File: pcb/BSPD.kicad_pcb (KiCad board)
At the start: 4 copper layers, 45 x 63.7 mm, 61 parts, among them J1 Test header, J2 T4142012121-000, Q1 AO3400A, U1 LM339, U2 LM339, U3 74HC32, U4 LM339, U5 L7805, U6 L7805, U8 74HC1G04GV,125

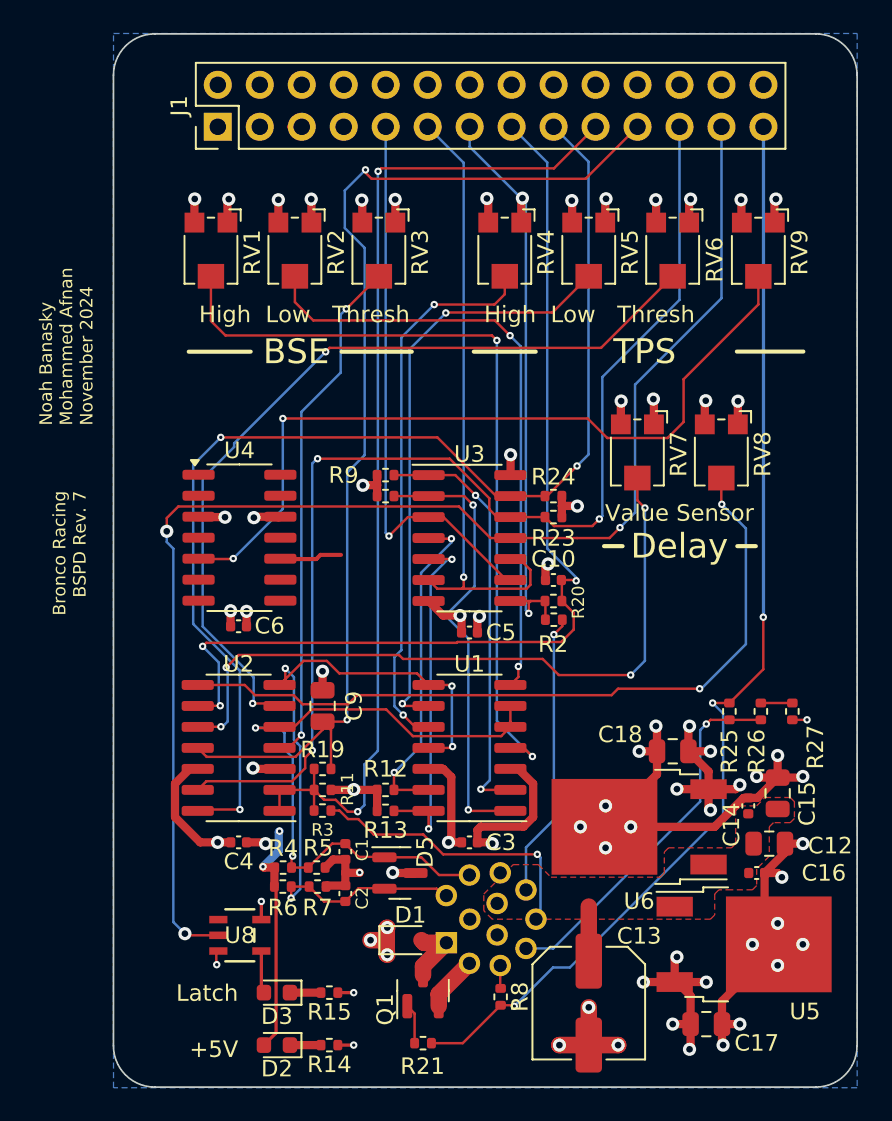
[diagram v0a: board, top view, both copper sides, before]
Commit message: change pcb layout
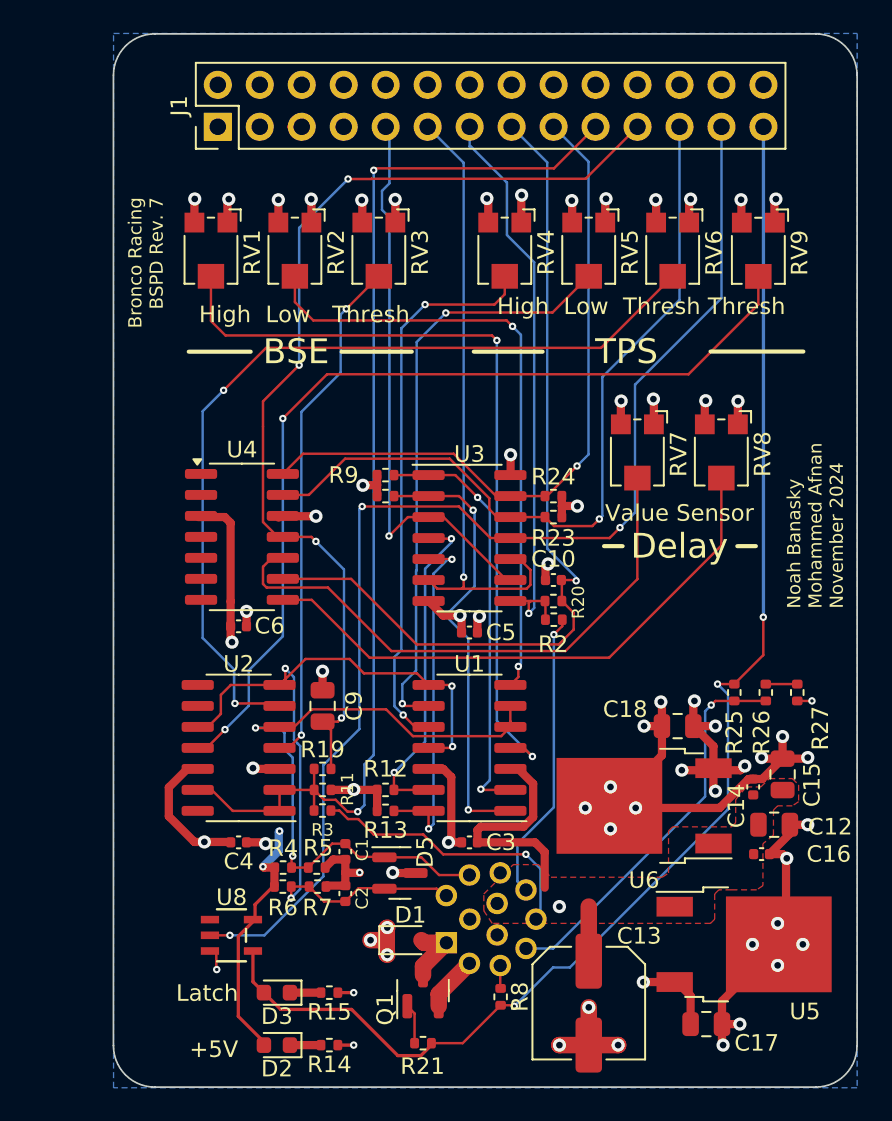
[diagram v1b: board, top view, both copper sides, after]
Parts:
- moved C18 1.55 mm to (146.6, 124.4)
- moved U6 1.31 mm to (144.6, 129.2)
- moved C12 1.18 mm to (152.5, 130.4)
- moved C14 1.18 mm to (151.2, 128.1)
- moved C15 1.18 mm to (153.0, 127.3)
- moved C16 1.18 mm to (151.7, 132.1)
- moved R25 1.18 mm to (150.1, 122.4)
- moved R26 1.18 mm to (152.0, 122.4)
- moved R27 1.18 mm to (153.9, 122.4)
- moved U8 0.51 mm to (119.6, 137.0)
- moved U4 0.16 mm to (120.3, 112.9)
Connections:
- U4 pad 10: SENSOR_DELAY -> VALUE_DELAY
- U4 pad 11: /Sensor Pre-Delay -> /Value Pre-Delay
- U4 pad 13: /Sensor Post-Delay -> /Value Post-Delay
- U4 pad 14: /Value Post-Delay -> /Sensor Post-Delay
- U4 pad 8: VALUE_DELAY -> SENSOR_DELAY
- U4 pad 9: /Value Pre-Delay -> /Sensor Pre-Delay
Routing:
- net Vin: track 24.9 -> 72.0 mm, vias 8 -> 7
- net /Sensor Post-Delay: track 71.3 -> 40.8 mm, vias 3 -> 1
- net /Value Post-Delay: track 70.4 -> 47.3 mm, vias 3 -> 1
- net SENSOR_DELAY: track 49.7 -> 34.9 mm, vias 2 -> 0
- net FAULT_5V: track 69.8 -> 82.1 mm
- net /Sensor Pre-Delay: track 61.5 -> 52.9 mm, vias 3 -> 1
- net Post-Delay: track 83.3 -> 74.6 mm
- net VALUE_DELAY: track 43.0 -> 34.7 mm, vias 4 -> 0
- net TPS_THRESH_NEGATIVE: track 47.7 -> 55.8 mm
- net TPS_in: track 43.4 -> 50.2 mm
- net Value Error: track 62.6 -> 68.3 mm
- net /Value Pre-Delay: track 66.4 -> 61.2 mm, vias 2 -> 4
- net TPS_THRESH: track 50.0 -> 52.9 mm
- net GND: track 101.6 -> 103.9 mm
- net FAULT_3V3: track 22.5 -> 23.7 mm
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- removed copper zone on In2.Cu, net Vin
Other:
- board text added: "High Low Thresh Thresh"

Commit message: Small changes to silkscreen and fixed drc
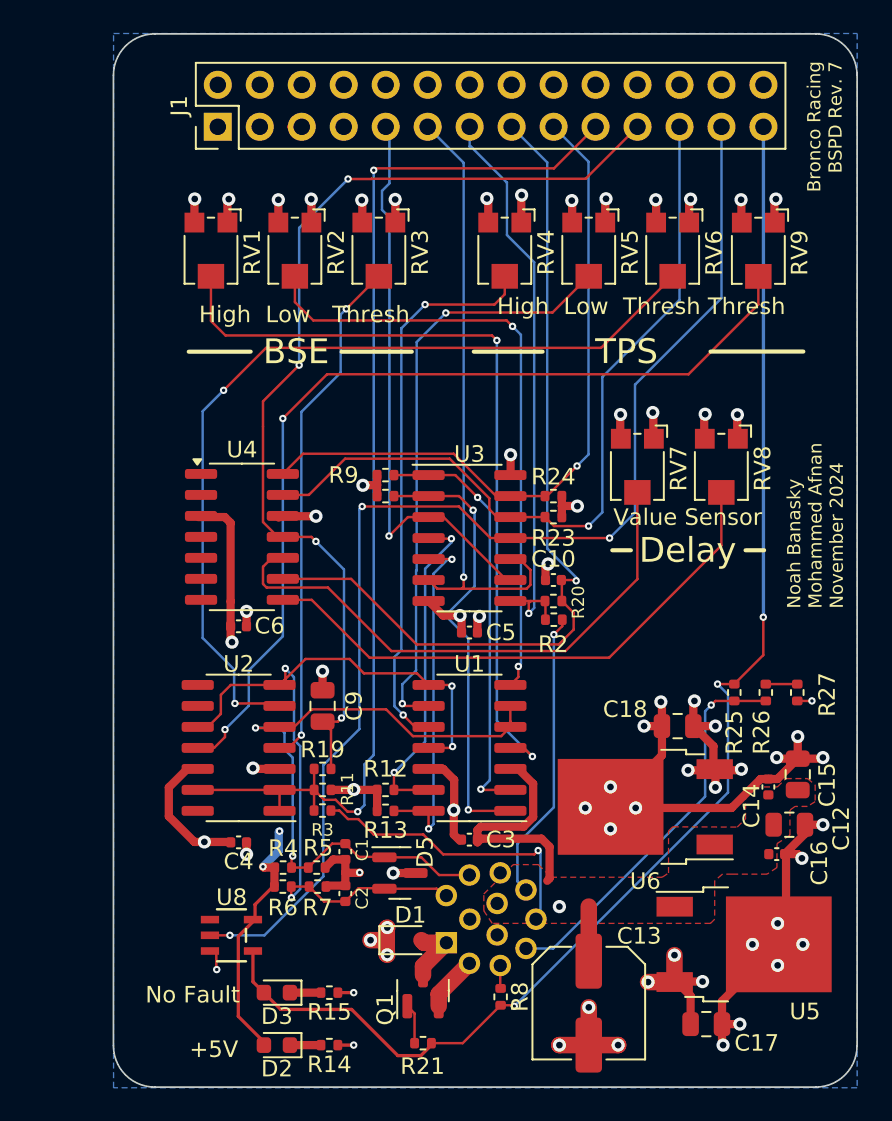
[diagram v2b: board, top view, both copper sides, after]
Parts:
- moved C12 0.92 mm to (153.4, 130.4)
- moved C14 0.92 mm to (152.1, 128.1)
- moved C15 0.92 mm to (153.9, 127.3)
- moved C16 0.92 mm to (152.6, 132.1)
- moved RV7 0.87 mm to (144.2, 108.8)
- moved RV8 0.87 mm to (149.3, 108.8)
- moved C3 0.17 mm to (134.0, 131.3)
- moved U6 0.10 mm to (144.7, 129.3)
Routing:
- net +5VE: track 11.8 -> 18.1 mm, vias 1 -> 3
- net Vin: track 72.0 -> 75.5 mm
- net +5V: track 51.9 -> 50.2 mm
- net VALUE_DELAY: track 34.7 -> 33.8 mm
- net SENSOR_DELAY: track 34.9 -> 34.0 mm
- net Net-(J2-Pad6): track 17.3 -> 18.1 mm
- net FAULT_5V: track 82.1 -> 81.5 mm
- net Value Error: track 68.3 -> 67.8 mm
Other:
- board text added: "No Fault"
- board text removed: "Latch"

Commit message: Design checklist changes
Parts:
- added D4: SMAJ15CA, Diode_SMD:D_SMA, F.Cu at (143.1, 132.9)
- moved C18 5.93 mm to (147.6, 118.5)
- moved U6 5.93 mm to (145.6, 123.4)
- moved R25 2.30 mm to (152.3, 122.7)
- moved R26 1.70 mm to (153.6, 122.7)
- moved R27 1.09 mm to (154.9, 122.7)
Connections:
- U2 pad 14: (no net) -> unconnected-(U2-Pad14)
- U2 pad 8: (no net) -> GND
- U2 pad 9: (no net) -> +5V
- U4 pad 1: (no net) -> unconnected-(U4-Pad1)
- U4 pad 2: (no net) -> unconnected-(U4-Pad2)
- U4 pad 4: (no net) -> GND
- U4 pad 5: (no net) -> +5V
- U4 pad 6: (no net) -> GND
- U4 pad 7: (no net) -> +5V
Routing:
- net GND: track 103.9 -> 115.7 mm, vias 42 -> 45
- net +5V: track 50.2 -> 56.1 mm, vias 21 -> 24
- net Vin: track 75.5 -> 81.3 mm
- net Value Error: track 67.8 -> 69.2 mm
- net SENSOR_DELAY: track 34.0 -> 32.8 mm
- net Net-(R26-Pad2): track 1.91 -> 1.28 mm
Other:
- board text added: "CS"
- board text removed: "TPS"

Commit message: Remove lck files
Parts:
- U8: footprint libraries:SOT23-5_FAS -> Package_TO_SOT_SMD:SOT-553

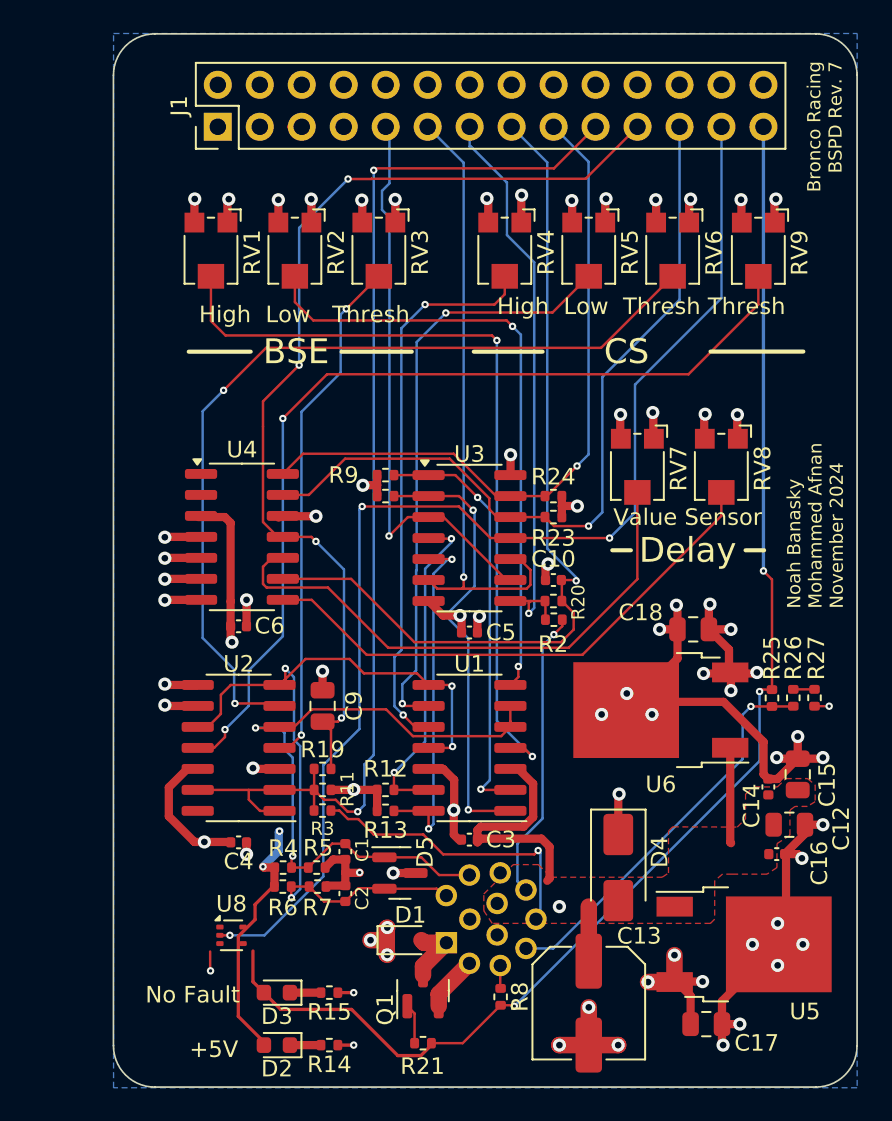
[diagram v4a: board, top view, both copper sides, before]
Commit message: trace routing improvements and fixed inverter mistake
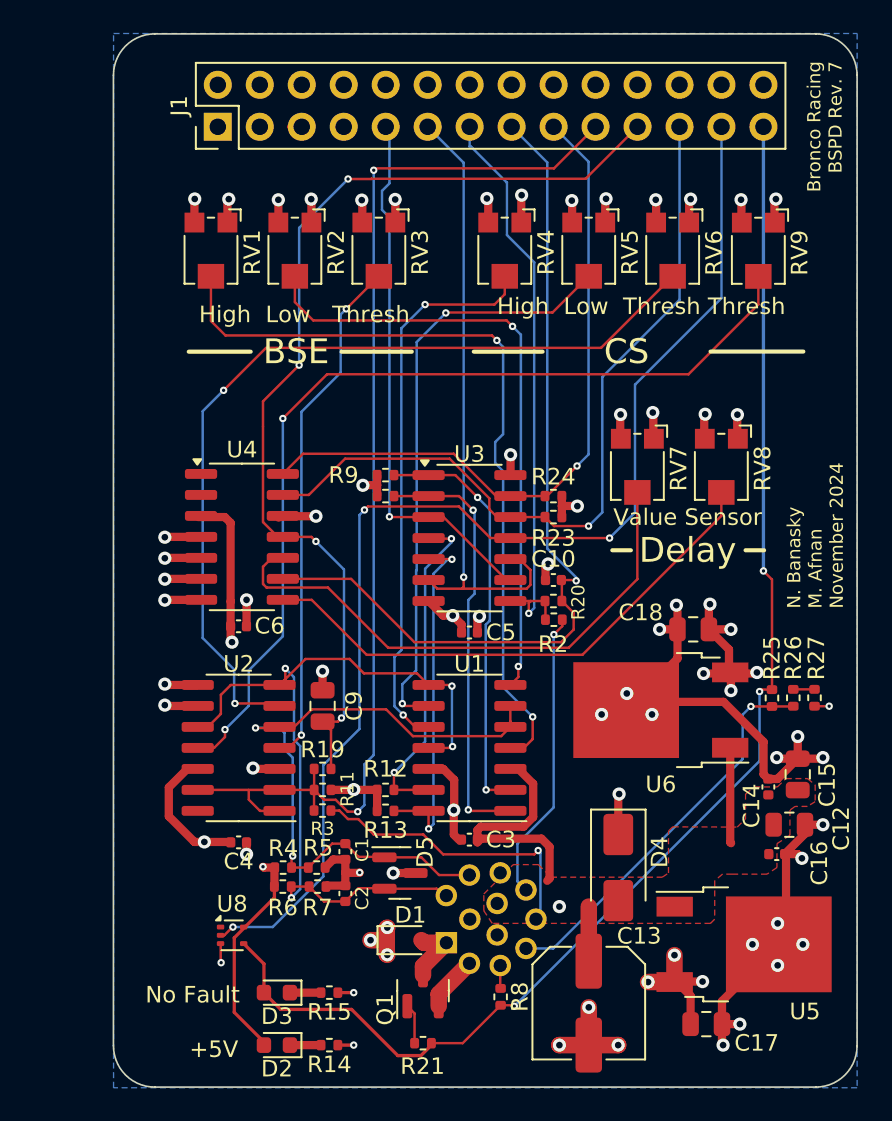
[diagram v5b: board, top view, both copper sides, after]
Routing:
- net +5V: track 56.1 -> 53.7 mm, vias 24 -> 23
- net BSE Error: track 34.4 -> 32.7 mm
- net Net-(R10-Pad1): track 27.0 -> 26.0 mm
- net FAULT_5V: track 81.1 -> 81.8 mm
- net BSE_HIGH: track 47.3 -> 46.7 mm
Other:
- board text added: "N. Banasky M. Afnan November 2024"
- board text removed: "Noah Banasky Mohammed Afnan November 2024"
